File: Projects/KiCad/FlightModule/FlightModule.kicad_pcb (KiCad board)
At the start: 2 copper layers, 110 x 95 mm, 62 parts, among them J1 Conn_01x08, J2 Conn_01x02_Pin, J3 Conn_01x02_Pin, J4 Conn_01x02_Pin, J5 Conn_01x02_Pin, J6 Conn_01x02_Pin, Q1 DTC143E, SW1 SW_Push, SW2 SW_Push, U1 MCP2562-E-P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

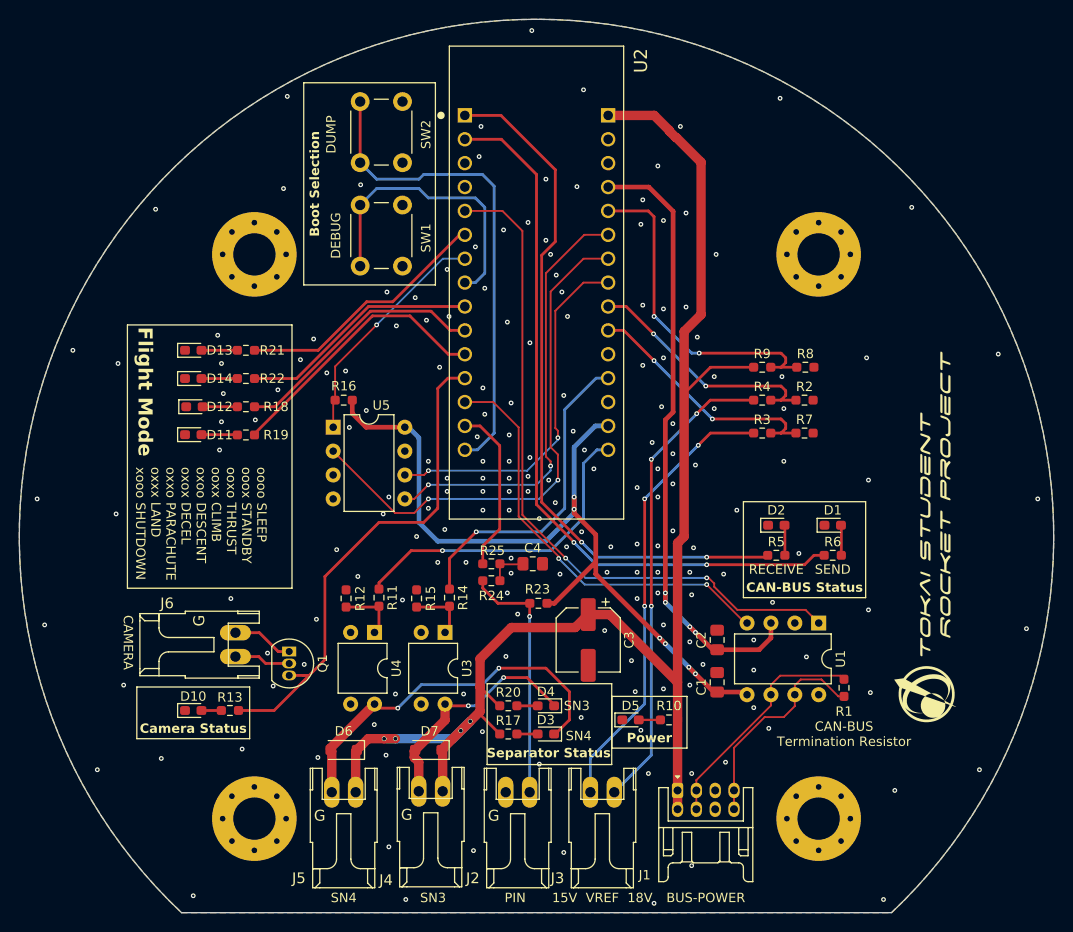
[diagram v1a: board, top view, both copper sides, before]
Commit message: 穴径を調整
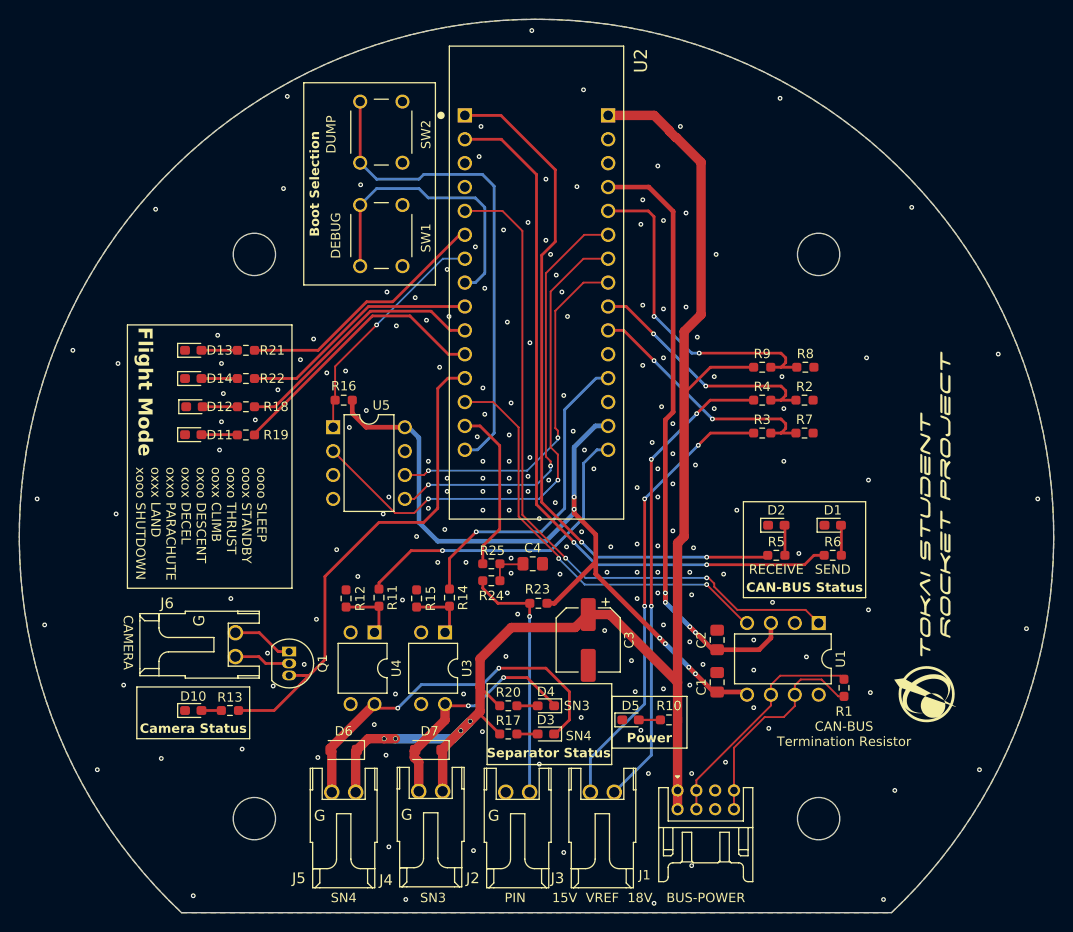
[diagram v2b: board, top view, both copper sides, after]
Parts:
- REF** (x3): value MountingHole_4.5mm_Pad_Via -> MountingHole_4.5mm; footprint MountingHole:MountingHole_4.5mm_Pad_Via -> MountingHole:MountingHole_4.5mm
- e: renamed from REF**; value MountingHole_4.5mm_Pad_Via -> MountingHole_4.5mm; footprint MountingHole:MountingHole_4.5mm_Pad_Via -> MountingHole:MountingHole_4.5mm

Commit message: テストポイントを追加
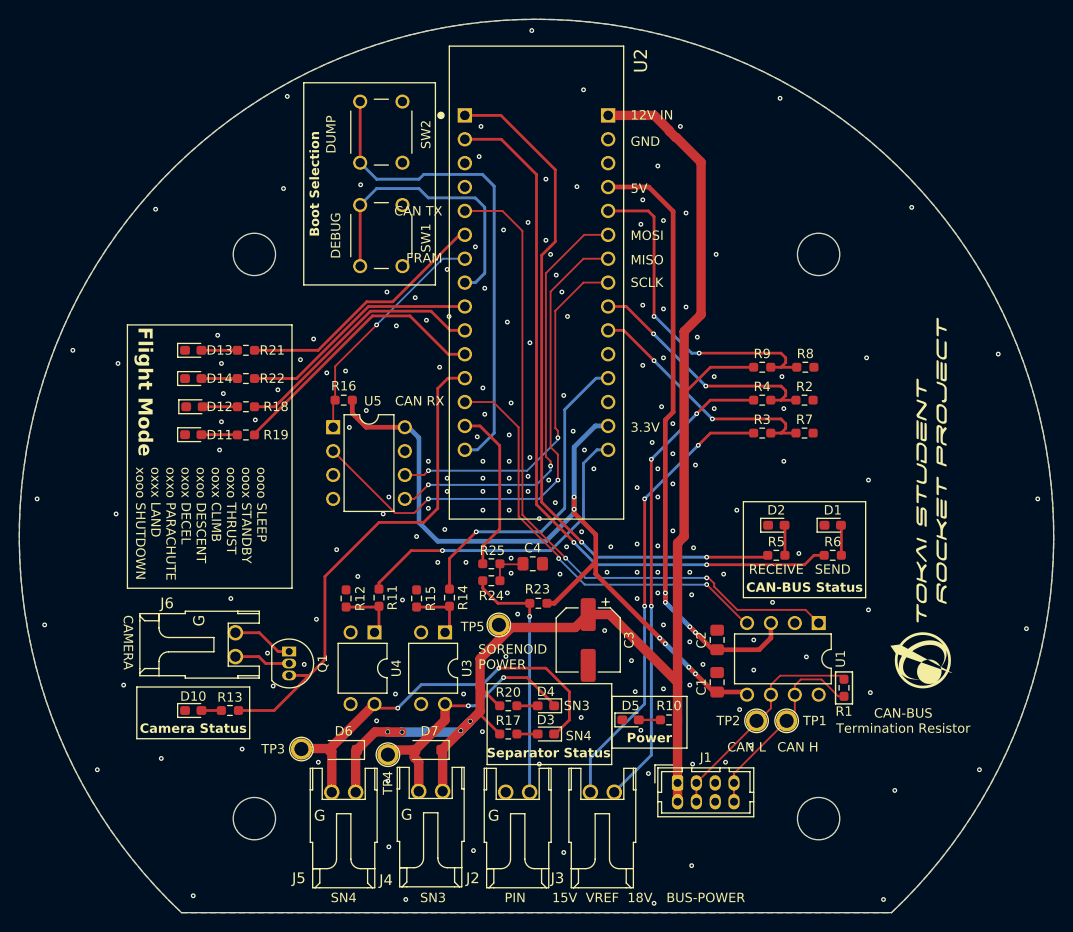
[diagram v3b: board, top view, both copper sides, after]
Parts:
- added TP1: TestPoint, Connector_Pin:Pin_D1.0mm_L10.0mm, F.Cu at (175.1, 124.6)
- added TP2: TestPoint, Connector_Pin:Pin_D1.0mm_L10.0mm, F.Cu at (171.9, 124.6)
- added TP3: TestPoint, Connector_Pin:Pin_D1.0mm_L10.0mm, F.Cu at (123.5, 127.6)
- added TP4: TestPoint, Connector_Pin:Pin_D1.0mm_L10.0mm, F.Cu at (132.7, 128.2)
- added TP5: TestPoint, Connector_Pin:Pin_D1.0mm_L10.0mm, F.Cu at (144.5, 114.4)
- J1: footprint Hirose_Connector:Hirose_DF11B-8DP-2DS -> Connector_Hirose:Hirose_DF11-8DP-2DSA_2x04_P2.00mm_Vertical
- moved G*** 3.62 mm to (189.5, 101.4)
- moved J1 0.80 mm to (163.5, 131.2)
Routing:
- net Net-(D3-K): track 40.3 -> 43.5 mm
- net Net-(D4-K): track 25.1 -> 28.2 mm
- net CAN_H: track 23.3 -> 21.3 mm
- net CAN_L: track 24.8 -> 24.0 mm
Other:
- board text added: "12V IN"
- board text added: "3.3V"
- board text added: "5V"
- board text added: "CAN H"
- board text added: "CAN L"
- board text added: "CAN RX"
- board text added: "CAN TX"
- board text added: "FRAM"
- board text added: "GND"
- board text added: "MISO"
- board text added: "MOSI"
- board text added: "SCLK"
- board text added: "SORENOID POWER"

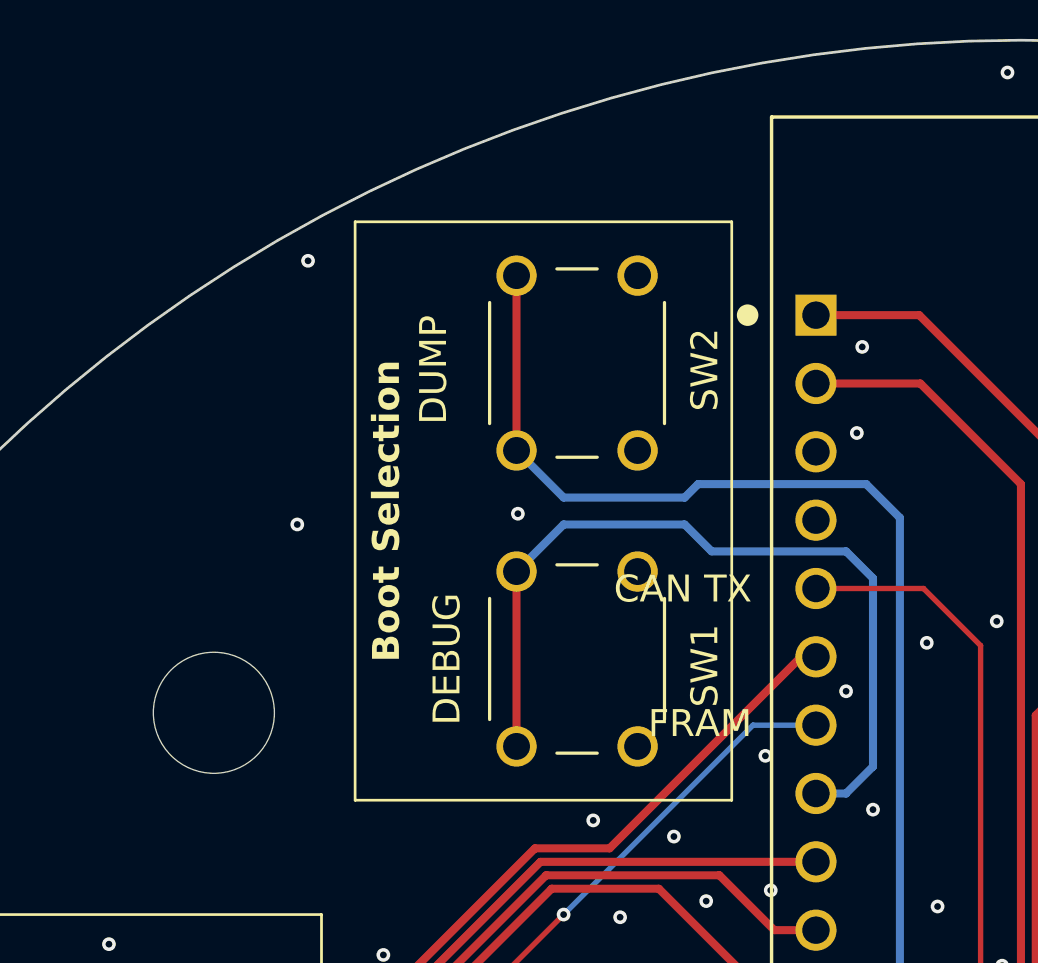
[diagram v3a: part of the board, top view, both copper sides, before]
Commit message: スイッチをピアノスイッチに変更
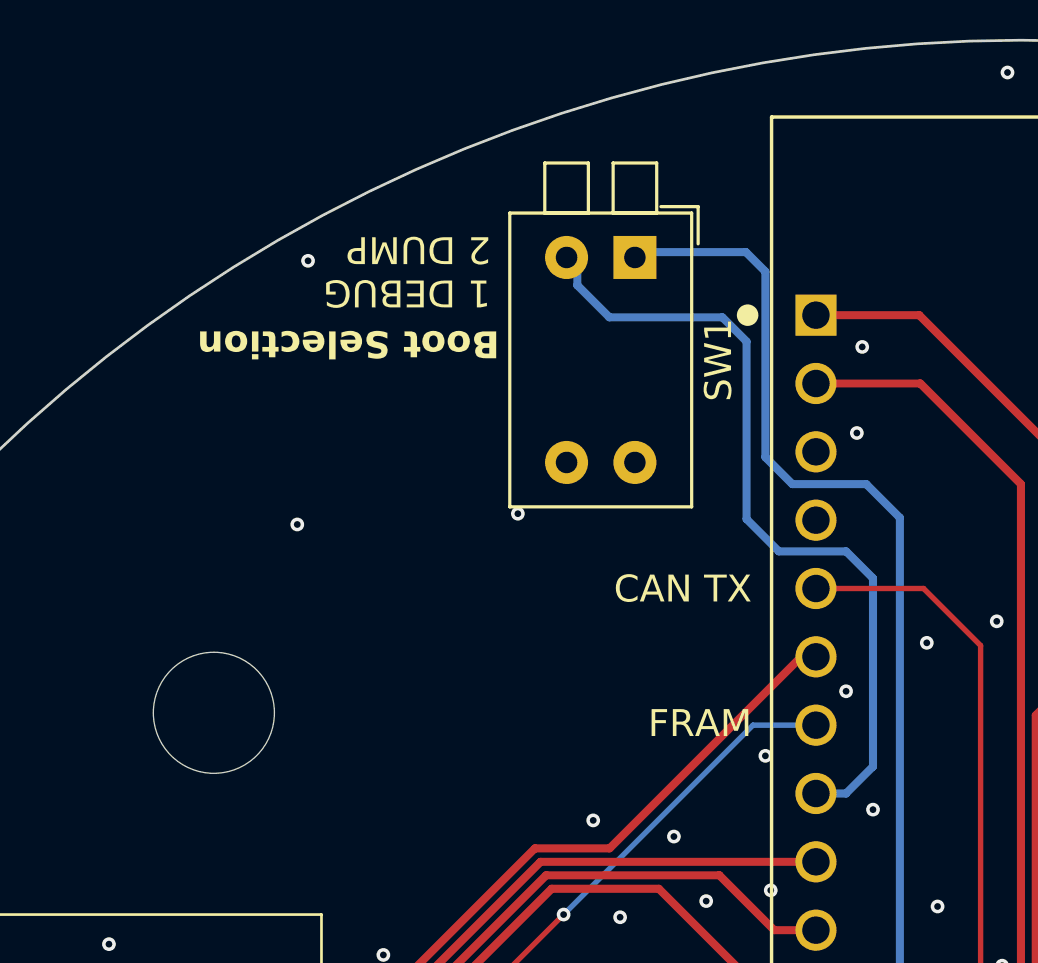
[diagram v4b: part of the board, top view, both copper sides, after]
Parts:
- removed SW2: SW_Push, Button_Switch_THT:SW_PUSH_6mm
- SW1: value SW_Push -> SW_DIP_x02; footprint Button_Switch_THT:SW_PUSH_6mm -> Button_Switch_THT:SW_DIP_SPSTx02_Piano_10.8x6.64mm_W7.62mm_P2.54mm
- moved SW1 11.7 mm to (134.2, 58.1)
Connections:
- SW1 pad 1: GND -> DEBUG_MODE
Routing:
- net DEBUG_MODE: track 52.3 -> 47.7 mm
- net DUMP_MODE: track 30.8 -> 30.1 mm
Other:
- board text added: "1 DEBUG 2 DUMP"
- board text removed: "DEBUG"
- board text removed: "DUMP"

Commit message: ベタを修正
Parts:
- moved D3 0.10 mm to (149.5, 126.1)
- moved R17 0.10 mm to (145.5, 126.1)
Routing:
- net Net-(R14-Pad2): track 6.68 -> 5.72 mm
- net Net-(R11-Pad2): track 6.52 -> 5.72 mm
- net CAN_L: track 24.0 -> 24.6 mm
- net GND: vias 186 -> 184

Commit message: 変圧基板を追加
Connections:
- net VOLTAGE_15V renamed VOLTAGE_BATT
- net VOLTAGE_18V renamed VOLTAGE_VSW
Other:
- board text added: "BATT"
- board text added: "VSW"
- board text removed: "15V"
- board text removed: "18V"
- board text removed: "BUS-POWER"

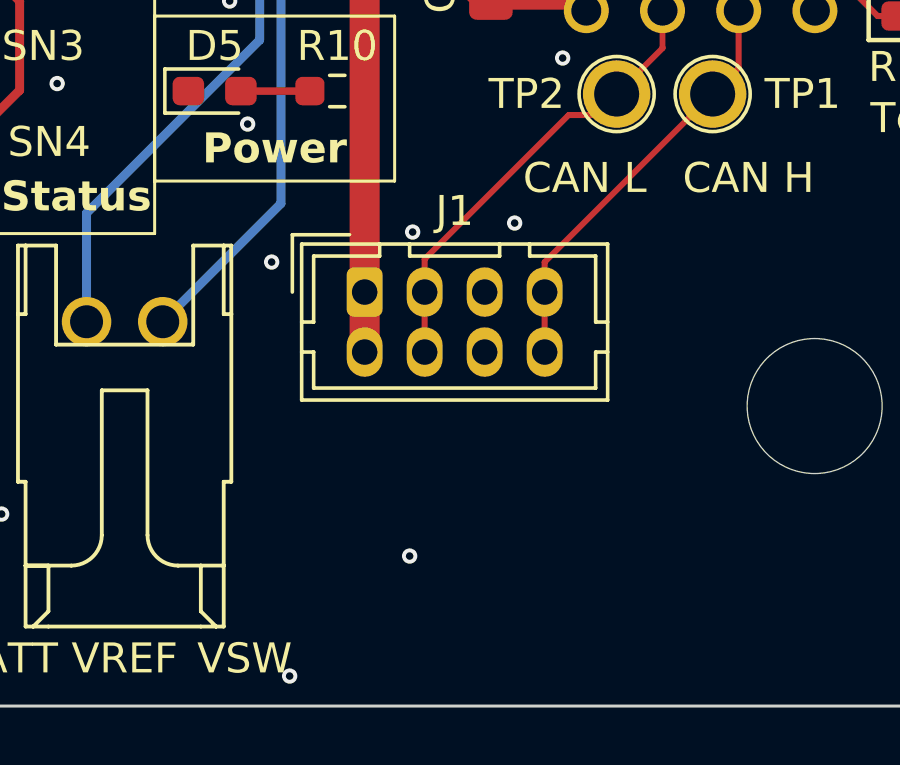
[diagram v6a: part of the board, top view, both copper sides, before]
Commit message: STEPファイルを再生成
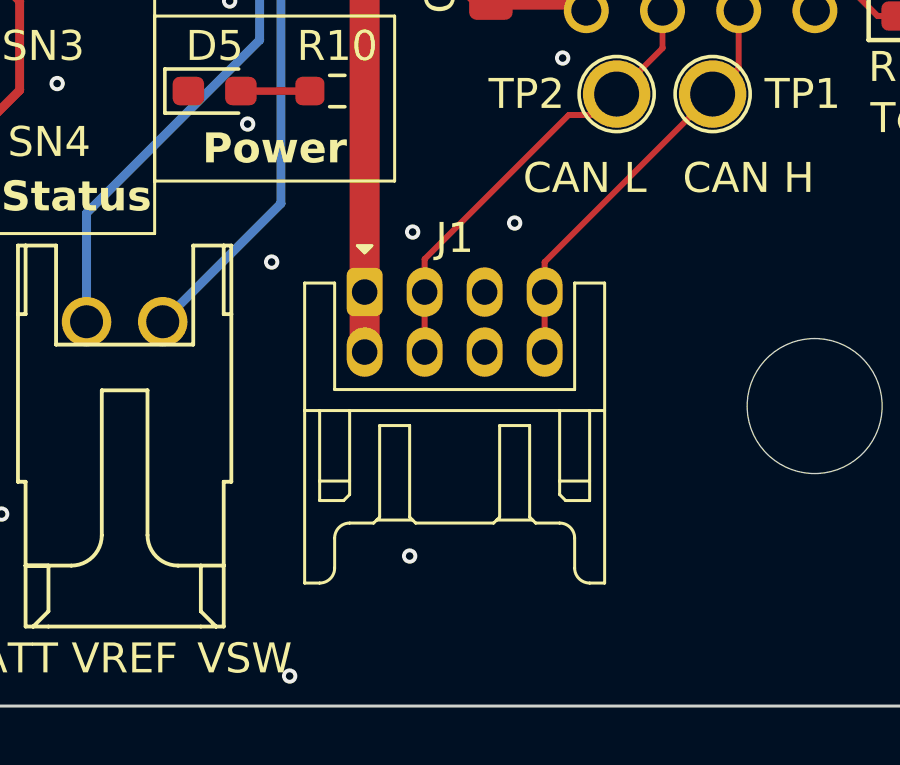
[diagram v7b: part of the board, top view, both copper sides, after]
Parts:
- J1: footprint Connector_Hirose:Hirose_DF11-8DP-2DSA_2x04_P2.00mm_Vertical -> Hirose_Connector:Hirose_DF11B-8DP-2DS
